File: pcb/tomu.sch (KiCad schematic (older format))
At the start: 22 parts, among them P1 USART0, P2 DEBUG, P3 USB-PCB, P4 RESET_PAD, P5 5V_PAD, P6 3V_PAD, U1 EFM32HG309

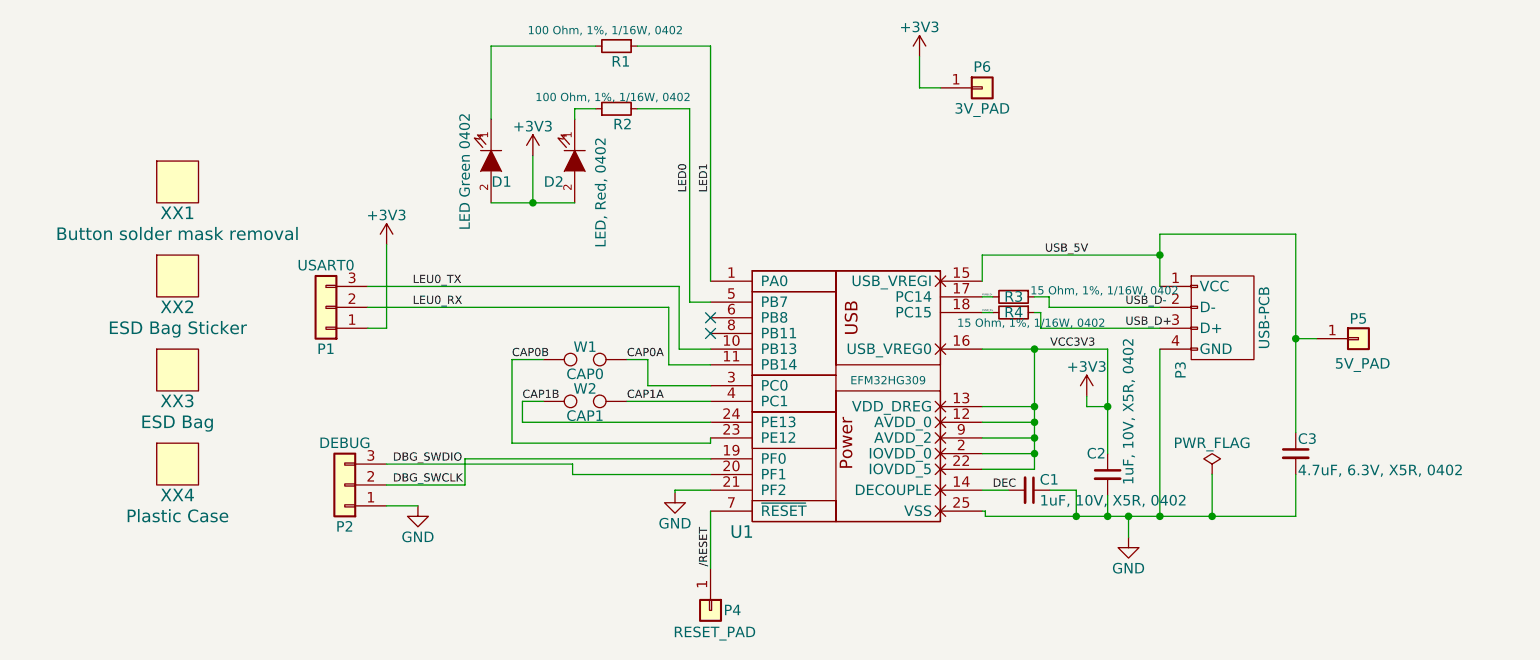
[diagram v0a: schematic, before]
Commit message: Add 2.54 pinhead version for easy developing
Signed-off-by: Zamir SUN <sztsian@gmail.com>
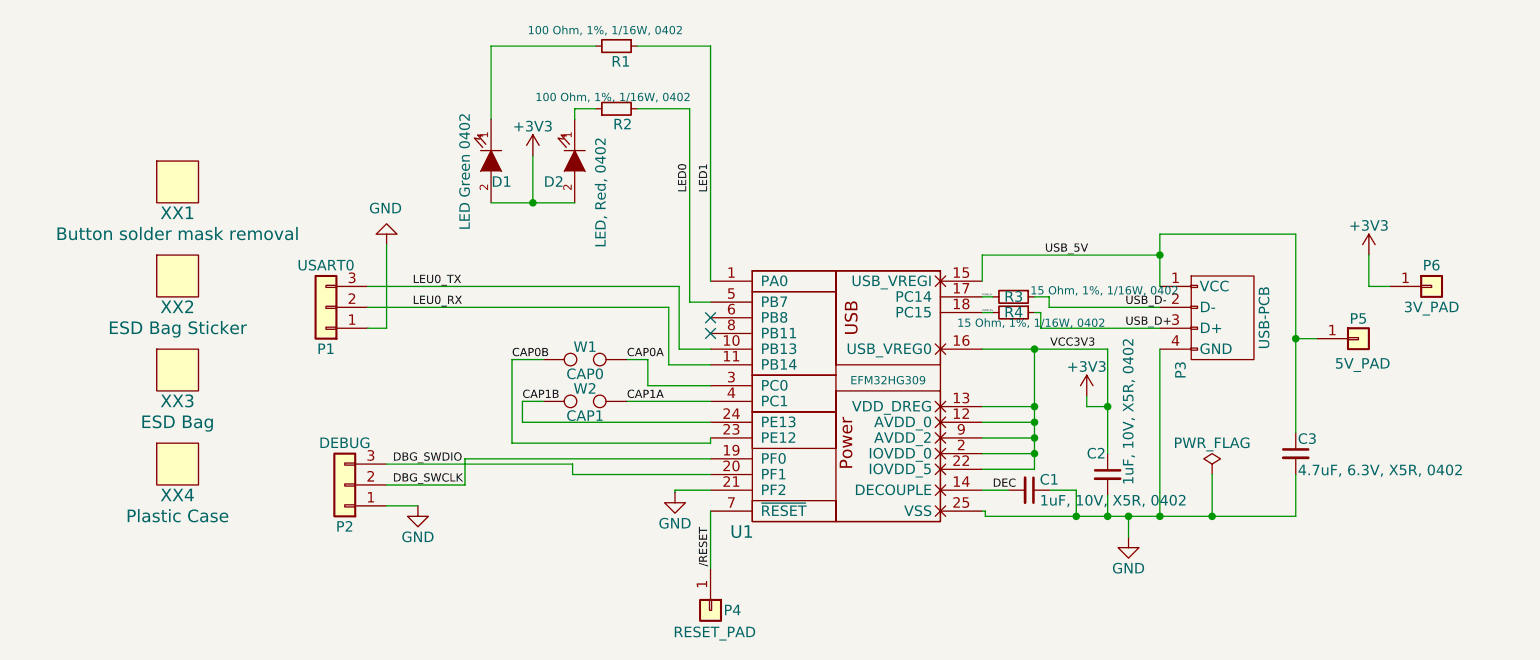
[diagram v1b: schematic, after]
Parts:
- C1, C2, C3: footprint Capacitors_SMD:C_0402 -> Capacitor_SMD:C_0603_1608Metric_Pad1.05x0.95mm_HandSolder
- D1, D2: footprint LEDs:LED_0402 -> LED_SMD:LED_0603_1608Metric_Pad1.05x0.95mm_HandSolder
- P1: footprint usb-pcb:pads-1x3-slim -> Connector_PinHeader_2.54mm:PinHeader_1x03_P2.54mm_Vertical
- P2: footprint usb-pcb:pads-1x3 -> Connector_PinHeader_2.54mm:PinHeader_1x03_P2.54mm_Vertical
- R1, R2, R3, R4: footprint Resistors_SMD:R_0402 -> Resistor_SMD:R_0603_1608Metric_Pad1.05x0.95mm_HandSolder
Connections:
- net +3V3: no longer P1.1 (Pin_1)
- net GND: now also P1.1 (Pin_1)
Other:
- moved on the sheet: P6
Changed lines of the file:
@@
 EESchema Schematic File Version 4
 LIBS:tomu-cache
-EELAYER 26 0
+EELAYER 29 0
 EELAYER END
 $Descr A4 11693 8268
@@
 F 0 "C2" H 6000 4050 50  0000 L CNN
 F 1 "1uF, 10V, X5R, 0402" V 6200 3900 50  0000 L CNN
-F 2 "Capacitors_SMD:C_0402" H 6100 3950 50  0001 C CNN
+F 2 "Capacitor_SMD:C_0603_1608Metric_Pad1.05x0.95mm_HandSolder" H 6100 3950 50  0001 C CNN
 F 3 "" H 6100 3950 50  0000 C CNN
 F 4 "ANY" H 6100 3950 50  0001 C CNN "MPN"
@@
 F 0 "C3" H 7010 3920 50  0000 L CNN
 F 1 "4.7uF, 6.3V, X5R, 0402" H 7010 3770 50  0000 L CNN
-F 2 "Capacitors_SMD:C_0402" H 7000 3850 50  0001 C CNN
+F 2 "Capacitor_SMD:C_0603_1608Metric_Pad1.05x0.95mm_HandSolder" H 7000 3850 50  0001 C CNN
 F 3 "" H 7000 3850 50  0000 C CNN
 F 4 "ANY" H 7000 3850 50  0001 C CNN "Manufacturer"
@@
 F 0 "C1" V 5675 4075 50  0000 L CNN
 F 1 "1uF, 10V, X5R, 0402" V 5775 4075 50  0000 L CNN
-F 2 "Capacitors_SMD:C_0402" H 5725 4025 50  0001 C CNN
+F 2 "Capacitor_SMD:C_0603_1608Metric_Pad1.05x0.95mm_HandSolder" H 5725 4025 50  0001 C CNN
 F 3 "" H 5725 4025 50  0000 C CNN
 F 4 "ANY" V 5725 4025 50  0001 C CNN "MPN"
@@
 F 0 "R3" V 5650 3055 50  0000 L CNN
 F 1 "15 Ohm, 1%, 1/16W, 0402" V 5620 3180 39  0000 L CNN
-F 2 "Resistors_SMD:R_0402" H 5650 3100 50  0001 C CNN
+F 2 "Resistor_SMD:R_0603_1608Metric_Pad1.05x0.95mm_HandSolder" H 5650 3100 50  0001 C CNN
 F 3 "" H 5650 3100 50  0000 C CNN
 F 4 "ANY" V 5650 3100 50  0001 C CNN "Manufacturer"
@@
 F 0 "R4" V 5650 3130 50  0000 L CNN
 F 1 "15 Ohm, 1%, 1/16W, 0402" V 5700 2905 39  0000 L CNN
-F 2 "Resistors_SMD:R_0402" H 5650 3175 50  0001 C CNN
+F 2 "Resistor_SMD:R_0603_1608Metric_Pad1.05x0.95mm_HandSolder" H 5650 3175 50  0001 C CNN
 F 3 "" H 5650 3175 50  0000 C CNN
 F 4 "ANY" V 5650 3175 50  0001 C CNN "Manufacturer"
@@
 F 0 "D1" V 3250 2500 50  0000 C CNN
 F 1 "LED Green 0402 " H 3200 2325 50  0000 C CNN
-F 2 "LEDs:LED_0402" H 3150 2450 50  0001 C CNN
+F 2 "LED_SMD:LED_0603_1608Metric_Pad1.05x0.95mm_HandSolder" H 3150 2450 50  0001 C CNN
 F 3 "" H 3150 2450 50  0000 C CNN
 F 4 "ANY" V 3150 2450 50  0001 C CNN "MPN"
@@
 F 0 "D2" V 3650 2350 50  0000 C CNN
 F 1 "LED, Red, 0402" H 3700 2575 50  0000 C CNN
-F 2 "LEDs:LED_0402" H 3550 2450 50  0001 C CNN
+F 2 "LED_SMD:LED_0603_1608Metric_Pad1.05x0.95mm_HandSolder" H 3550 2450 50  0001 C CNN
 F 3 "" H 3550 2450 50  0000 C CNN
 F 4 "ANY" V 3550 2450 50  0001 C CNN "Manufacturer"
@@
 F 0 "R2" V 3675 2125 50  0000 L CNN
 F 1 "100 Ohm, 1%, 1/16W, 0402" V 3805 1845 39  0000 L CNN
-F 2 "Resistors_SMD:R_0402" H 3750 2200 50  0001 C CNN
+F 2 "Resistor_SMD:R_0603_1608Metric_Pad1.05x0.95mm_HandSolder" H 3750 2200 50  0001 C CNN
 F 3 "" H 3750 2200 50  0000 C CNN
 F 4 "ANY" V 3750 2200 50  0001 C CNN "MPN"
@@
 F 0 "R1" V 3825 1875 50  0000 L CNN
 F 1 "100 Ohm, 1%, 1/16W, 0402" V 3675 1475 39  0000 L CNN
-F 2 "Resistors_SMD:R_0402" H 3750 1900 50  0001 C CNN
+F 2 "Resistor_SMD:R_0603_1608Metric_Pad1.05x0.95mm_HandSolder" H 3750 1900 50  0001 C CNN
 F 3 "" H 3750 1900 50  0000 C CNN
 F 4 "ANY" V 3750 1900 50  0001 C CNN "MPN"
@@
 	1    3750 1900
 	0    1    1    0
-$EndComp
-$Comp
-L power:+3V3 #PWR01
-U 1 1 5798FD73
-P 2650 2850
-F 0 "#PWR01" H 2650 2700 50  0001 C CNN
-F 1 "+3V3" H 2650 2990 50  0000 C CNN
-F 2 "" H 2650 2850 50  0000 C CNN
-F 3 "" H 2650 2850 50  0000 C CNN
-	1    2650 2850
-	1    0    0    -1
 $EndComp
 $Comp
@@
 $EndComp
 $Comp
-L tomu-rescue:Conn_01x03 P2
-U 1 1 5A55837D
-P 2450 4000
-F 0 "P2" H 2450 4200 50  0000 C CNN
-F 1 "DEBUG" H 2450 3800 50  0000 C CNN
-F 2 "usb-pcb:pads-1x3" H 2450 4000 50  0001 C CNN
-F 3 "" H 2450 4000 50  0001 C CNN
-F 4 "DNP" H 2450 4000 60  0001 C CNN "Notes"
-F 5 "Test points for SWD" H 2450 4000 60  0001 C CNN "Description"
-	1    2450 4000
-	-1   0    0    1
-$EndComp
-$Comp
 L power:PWR_FLAG #FLG01
 U 1 1 5A55865E
@@
 F 0 "P1" H 2360 3350 50  0000 C CNN
 F 1 "USART0" H 2360 2950 50  0000 C CNN
-F 2 "usb-pcb:pads-1x3-slim" H 2360 3150 50  0001 C CNN
+F 2 "Connector_PinHeader_2.54mm:PinHeader_1x03_P2.54mm_Vertical" H 2360 3150 50  0001 C CNN
 F 3 "" H 2360 3150 50  0001 C CNN
 F 4 "DNP" H 2360 3150 60  0001 C CNN "Notes"
@@
 Wire Wire Line
 	2650 3250 2560 3250
-$Comp
-L tomu-rescue:Conn_01x01 P6
-U 1 1 5A7007C6
-P 5500 2100
-F 0 "P6" H 5500 2200 50  0000 C CNN
-F 1 "3V_PAD" H 5500 2000 50  0000 C CNN
-F 2 "usb-pcb:pads-1x1" H 5500 2100 50  0001 C CNN
-F 3 "" H 5500 2100 50  0001 C CNN
-F 4 "DNP" H 5500 2100 60  0001 C CNN "Notes"
-F 5 "Test point for 3.3V power" H 5500 2100 60  0001 C CNN "Description"
-	1    5500 2100
-	1    0    0    -1
-$EndComp
-$Comp
-L power:+3V3 #PWR05
-U 1 1 5A7008F7
-P 5200 1950
-F 0 "#PWR05" H 5200 1800 50  0001 C CNN
-F 1 "+3V3" H 5200 2090 50  0000 C CNN
-F 2 "" H 5200 1950 50  0001 C CNN
-F 3 "" H 5200 1950 50  0001 C CNN
-	1    5200 1950
-	1    0    0    -1
-$EndComp
-Wire Wire Line
-	5200 1950 5200 2100
-Wire Wire Line
-	5200 2100 5300 2100
 Wire Wire Line
 	5750 3350 6100 3350
@@
 	1    0    0    -1
 $EndComp
+Wire Wire Line
+	7350 3050 7450 3050
+Wire Wire Line
+	7350 2900 7350 3050
+$Comp
+L tomu-rescue:Conn_01x01 P6
+U 1 1 5A7007C6
+P 7650 3050
+F 0 "P6" H 7650 3150 50  0000 C CNN
+F 1 "3V_PAD" H 7650 2950 50  0000 C CNN
+F 2 "usb-pcb:pads-1x1" H 7650 3050 50  0001 C CNN
+F 3 "" H 7650 3050 50  0001 C CNN
+F 4 "DNP" H 7650 3050 60  0001 C CNN "Notes"
+F 5 "Test point for 3.3V power" H 7650 3050 60  0001 C CNN "Description"
+	1    7650 3050
+	1    0    0    -1
+$EndComp
+$Comp
+L power:+3V3 #PWR05
+U 1 1 5A7008F7
+P 7350 2900
+F 0 "#PWR05" H 7350 2750 50  0001 C CNN
+F 1 "+3V3" H 7350 3040 50  0000 C CNN
+F 2 "" H 7350 2900 50  0001 C CNN
+F 3 "" H 7350 2900 50  0001 C CNN
+	1    7350 2900
+	1    0    0    -1
+$EndComp
+$Comp
+L tomu-rescue:Conn_01x03 P2
+U 1 1 5A55837D
+P 2450 4000
+F 0 "P2" H 2450 4200 50  0000 C CNN
+F 1 "DEBUG" H 2450 3800 50  0000 C CNN
+F 2 "Connector_PinHeader_2.54mm:PinHeader_1x03_P2.54mm_Vertical" H 2450 4000 50  0001 C CNN
+F 3 "" H 2450 4000 50  0001 C CNN
+F 4 "DNP" H 2450 4000 60  0001 C CNN "Notes"
+F 5 "Test points for SWD" H 2450 4000 60  0001 C CNN "Description"
+	1    2450 4000
+	-1   0    0    1
+$EndComp
+$Comp
+L power:GND #PWR0101
+U 1 1 5D2DBB2B
+P 2650 2850
+F 0 "#PWR0101" H 2650 2600 50  0001 C CNN
+F 1 "GND" H 2655 2677 50  0000 C CNN
+F 2 "" H 2650 2850 50  0001 C CNN
+F 3 "" H 2650 2850 50  0001 C CNN
+	1    2650 2850
+	-1   0    0    1
+$EndComp
 $EndSCHEMATC
